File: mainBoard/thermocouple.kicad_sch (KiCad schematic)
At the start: 57 parts, among them J4 4DB-P108-02, J5 4DB-P108-02, J6 4DB-P108-02, U10 DS18B20+, U11 DS18B20+, U12 OPA333AIDCKT, U13 DS18B20+, U8 OPA333AIDCKT, U9 OPA333AIDCKT

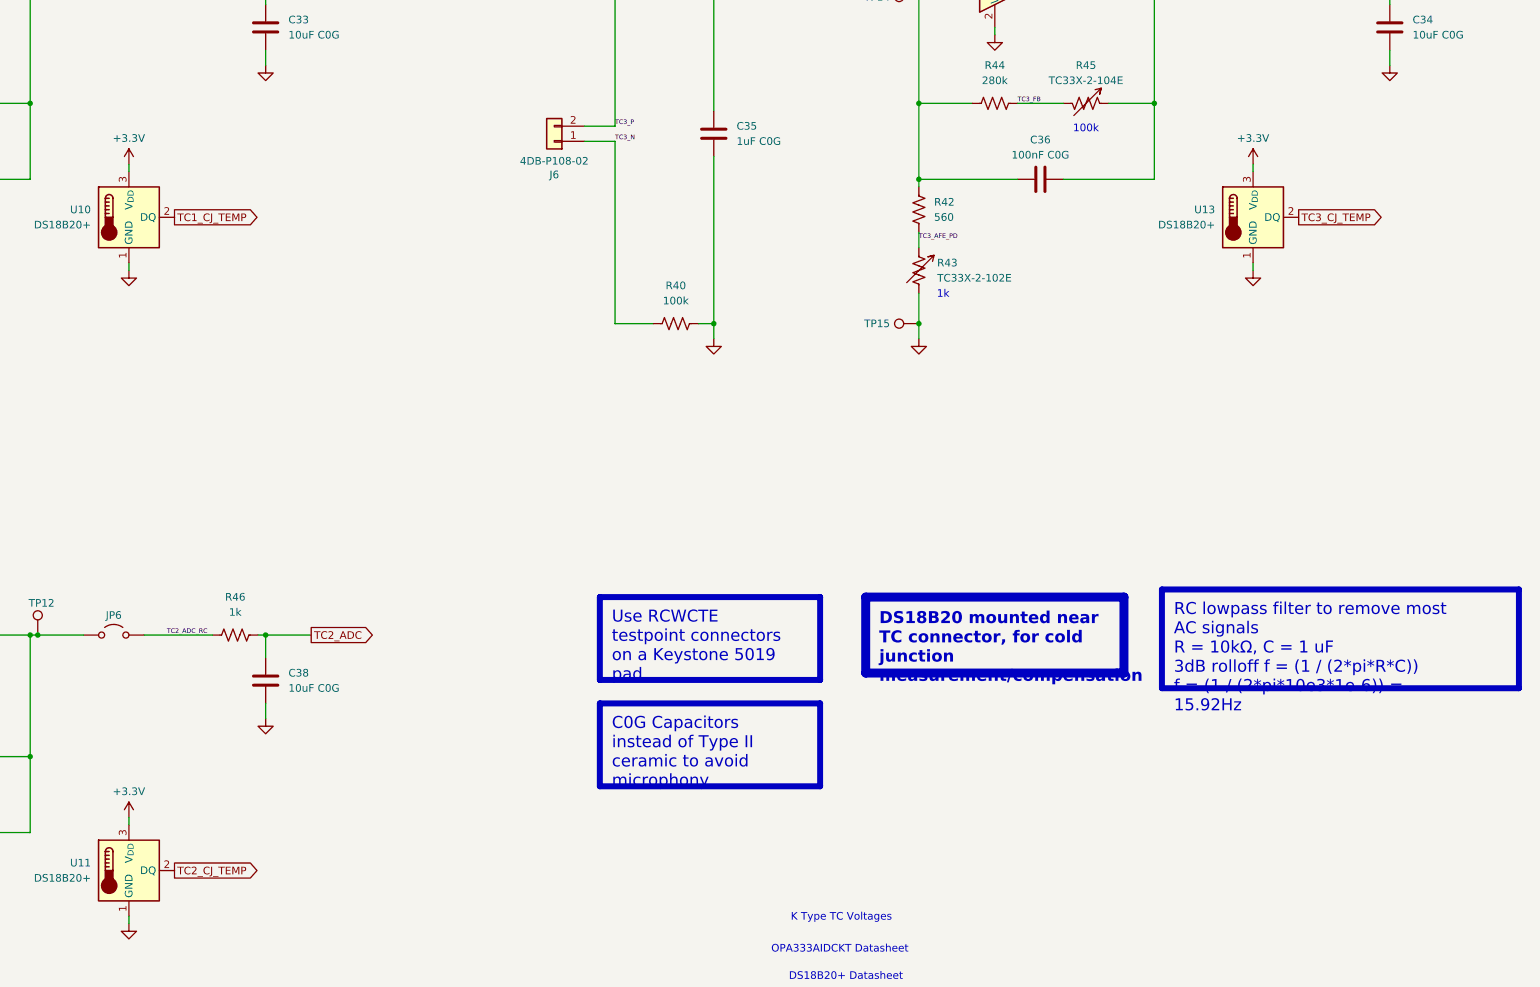
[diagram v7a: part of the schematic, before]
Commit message: Add pullup resistors to digital thermometers
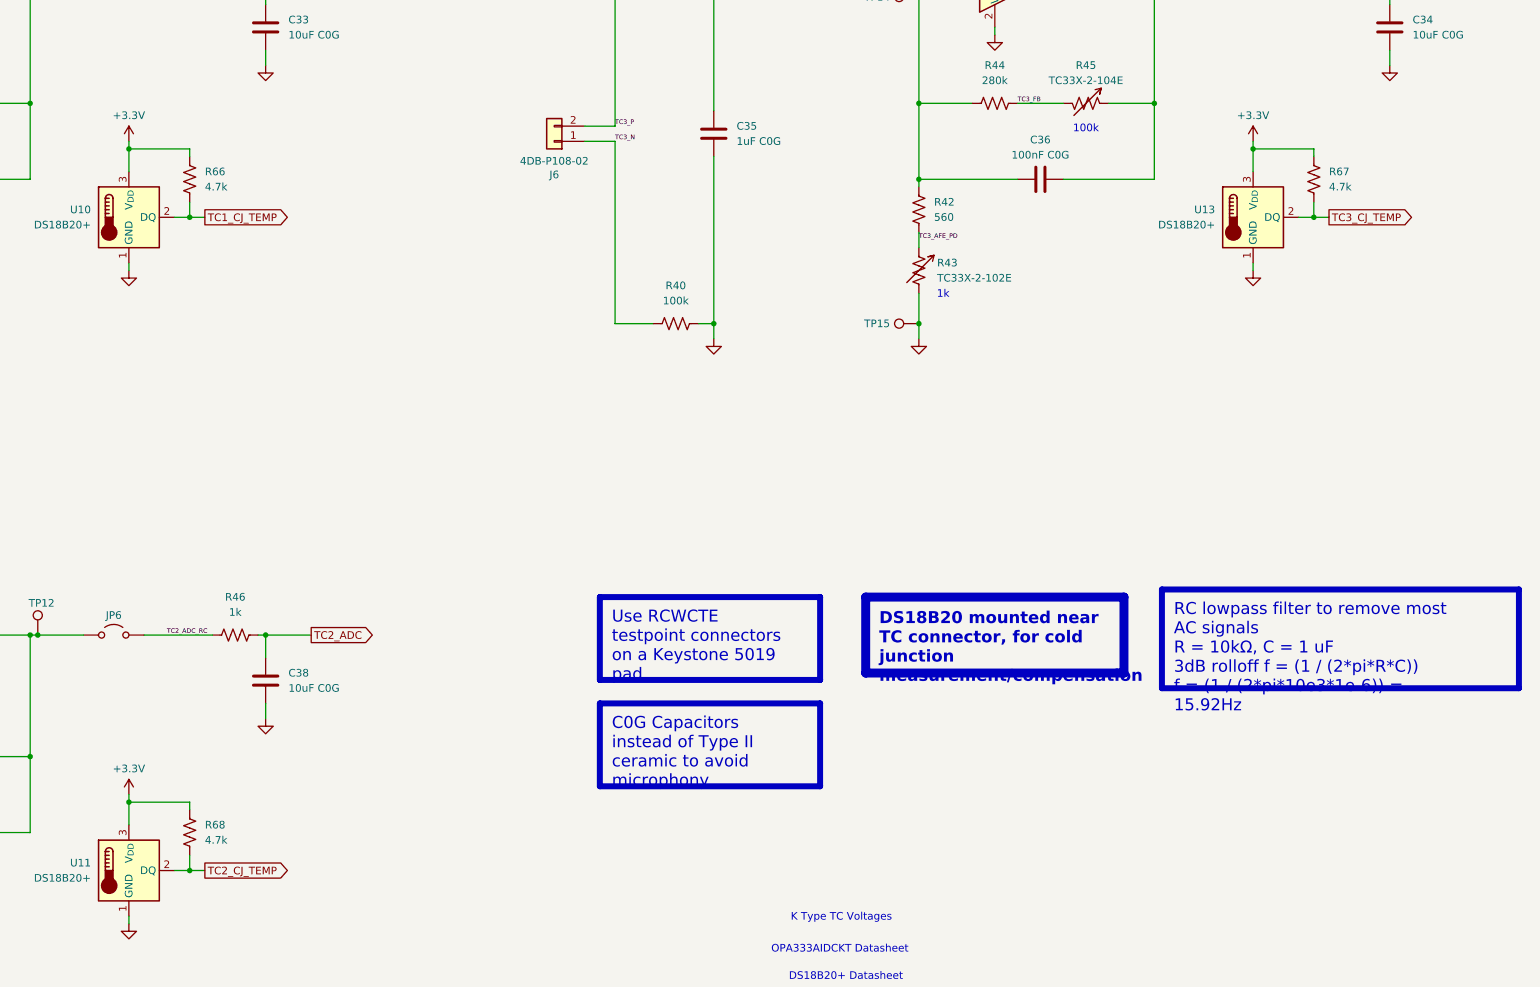
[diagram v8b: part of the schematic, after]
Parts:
- added R66, R67, R68: 4.7k, Resistor_SMD:R_0603_1608Metric_Pad0.98x0.95mm_HandSolder, symbol Device:R_US
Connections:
- net +3.3V: now also R66.1, R67.1, R68.1
- net TC1_CJ_TEMP: now also R66.2
- net TC2_CJ_TEMP: now also R68.2
- net TC3_CJ_TEMP: now also R67.2
